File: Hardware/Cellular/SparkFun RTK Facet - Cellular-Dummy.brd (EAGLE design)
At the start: 60 x 30.7 mm, 69 parts, among them IC1 SN74AVC4T774PW, J18 SARA_USB, J2 NANO_SIM, J3 U.FL, J6 DIAG, Q2 310mA/60V/1.6Ω, Q3 310mA/60V/1.6Ω, Q4 310mA/60V/1.6Ω, Q5 20V/0.2A/8MHz/1.2Ω/1Vth, Q7 310mA/60V/1.6Ω, U1 SARA-R510M8S, U8 74HC1G04

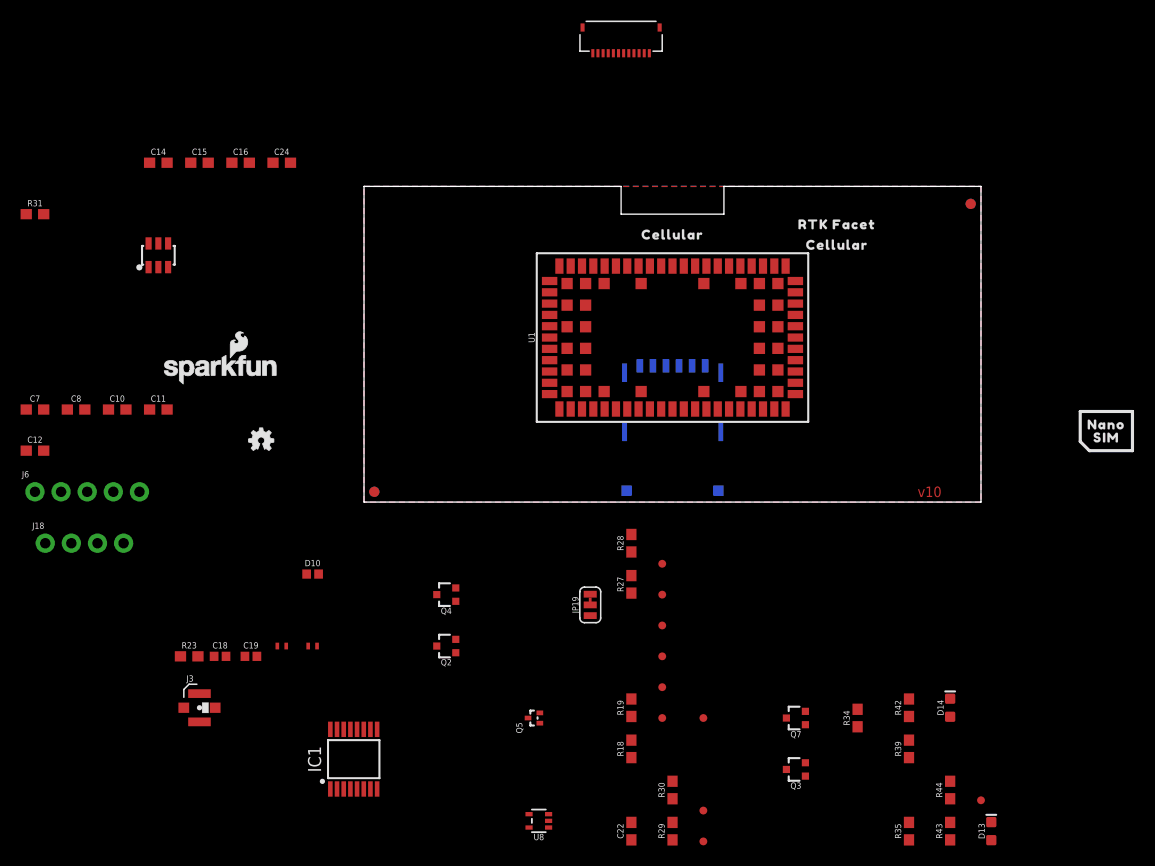
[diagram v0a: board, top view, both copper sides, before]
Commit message: Double up 3.3V on cell connector. Create dummy test board.
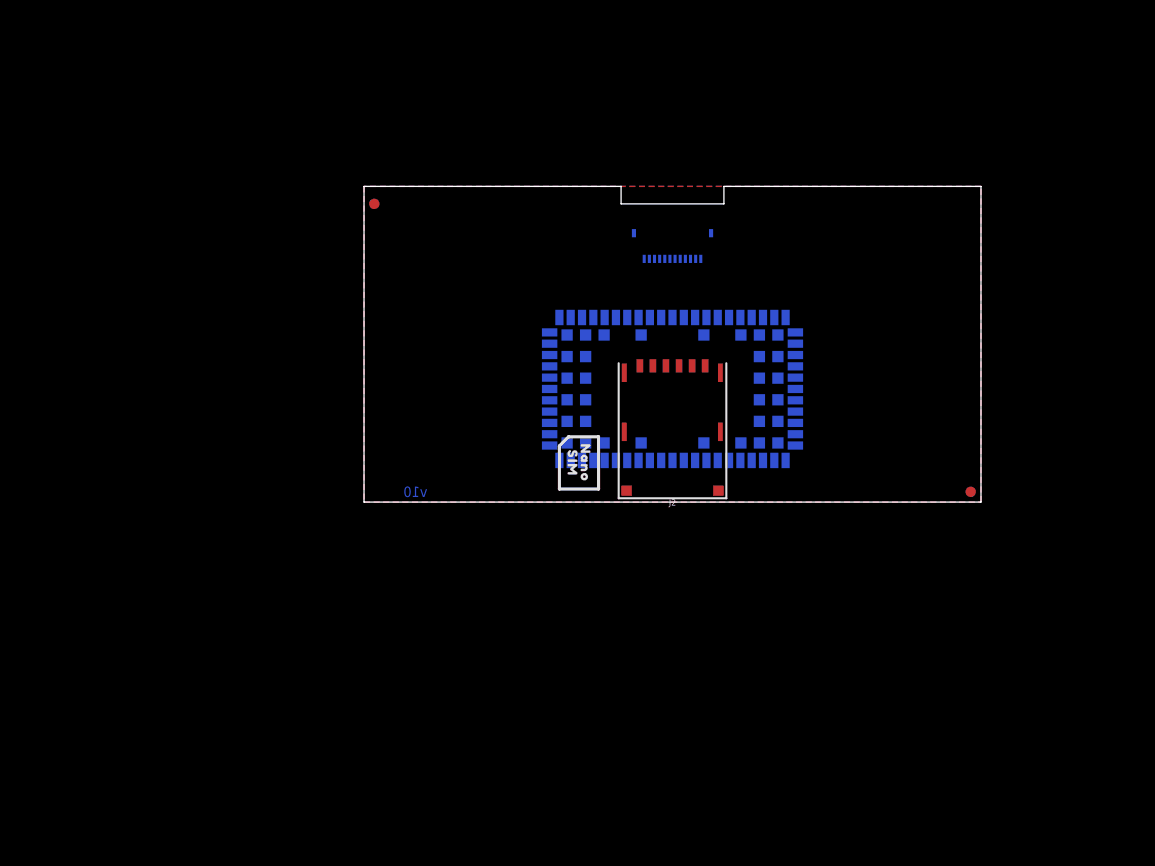
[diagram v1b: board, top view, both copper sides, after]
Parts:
- removed C10, C11, C7, C8: 47pF, SparkFun-Capacitors:0603
- removed C12, C14, C22: 0.1uF, SparkFun-Capacitors:0603
- removed C15: 68pF, SparkFun-Capacitors:0603
- removed C16: 10uF, SparkFun-Capacitors:0603
- removed C18: 33pF, New_Parts:0402
- removed C19: 27pF, New_Parts:0402
- removed C24: 15pF, SparkFun-Capacitors:0603
- removed D10: PESD0402, New_Parts:0402
- removed D13: BLUE, SparkFun-LED:LED-0603
- removed D14: WHITE, SparkFun-LED:LED-0603
- removed D8: DT1042-04SO-7, ublox:SOT23-6L
- removed FRAME2: FRAME-LETTERNO_PACKAGE, SparkFun-Aesthetics:DUMMY
- removed IC1: SN74AVC4T774PW, New_Parts:SOP65P640X120-16N
- removed J18: SARA_USB, SparkFun-Connectors:1X04_NO_SILK
- removed J3: U.FL, SparkFun-Connectors:U.FL
- removed J6: DIAG, SparkFun-Connectors:1X05_NO_SILK
- removed JP19: JUMPER-SMT_3_1-NC_TRACE_SILK, SparkFun-Jumpers:SMT-JUMPER_3_1-NC_TRACE_SILK
- removed L1: DNP, New_Parts:0402_COILCRAFT
- removed L2: 68nH, New_Parts:0402_COILCRAFT
- removed Q2, Q3, Q4, Q7: 310mA/60V/1.6Ω, SparkFun-DiscreteSemi:SOT323
- removed Q5: 20V/0.2A/8MHz/1.2Ω/1Vth, SparkFun-DiscreteSemi:SOT-416FL
- removed R18, R19, R39, R44: 100k, SparkFun-Resistors:0603
- removed R23: 10k, SparkFun-Resistors:0603
- removed R27, R28, R34, R42, R43: 1k, SparkFun-Resistors:0603
- removed R29, R30: 2.2k, SparkFun-Resistors:0603
- removed R31: 0, SparkFun-Resistors:0603
- removed R35: 470, SparkFun-Resistors:0603
- removed TP1, TP12, TP13, TP2, TP3, TP4, TP5, TP6, TP7, TP8: TEST-POINT3, SparkFun-Connectors:PAD.03X.03
- removed U8: 74HC1G04, SparkFun-IC-Logic:SOT353
- J2: value NANO_SIM -> (none); device ublox:NANO_SIM_WURTH_693043020611 -> SparkFun-Connectors:NANO_SIM_WURTH_693043020611
- moved LOGO5 65.9 mm to (50.9, 24.9), flipped to the bottom
- moved LOGO3 64.0 mm to (54.0, 5.00), flipped to the bottom
- moved FID1 58.0 mm to (59.0, 1.00), flipped to the top
- moved FID2 58.0 mm to (1.00, 29.0), flipped to the top
- moved FID3 58.0 mm to (1.00, 29.0), flipped to the bottom
- moved FID4 58.0 mm to (59.0, 1.00), flipped to the bottom
- moved U$131 52.0 mm to (20.3, 3.81), turned to 270 degrees
- moved U$130 50.8 mm to (21.5, 3.81), turned to 270 degrees
- moved FRAME1 45.1 mm to (7.43, -29.5), flipped to the top
- moved U$14 32.0 mm to (14.0, 27.0), flipped to the bottom
- moved U$2 32.0 mm to (14.0, 25.0), flipped to the bottom
- moved J1 20.6 mm to (30.0, 25.0), flipped to the bottom
- moved U1 5.00 mm to (30.0, 11.0), flipped to the bottom
- moved U$13 4.00 mm to (30.0, 22.0), flipped to the bottom
- flipped J2 to the top
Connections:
- removed net 1.8V: J6.4
- removed net LTE_NI: Q3.3, R35.1, R39.1
- removed net N$15: C18.2, J3.FEED, L2.P$2
- removed net N$16: C19.1, D10.1, L2.P$1, R23.2
- removed net N$26: Q2.1, R27.2
- removed net N$27: Q4.1, R28.2
- removed net N$28: R28.1, U8.4
- removed net N$31: R31.2, U1.4
- removed net N$35: Q3.1, R34.2
- removed net N$37: D13.C, R35.2
- removed net N$43: JP19.2, Q5.2, R29.1
- removed net N$47: Q7.1, R42.2
- removed net N$49: D14.C, R43.2
- removed net SARA_!ON!: Q7.3, R43.1, R44.1, TP13.P$1
- removed net SARA_GPIO3: JP19.1
- removed net VCCIO: C22.1, IC1.1, IC1.16, IC1.7, J6.3, Q5.1, R29.2, R31.1, R42.1
- removed net VIN: J6.1
- new net VCC: J2.C1, U1.51, U1.52, U1.53
- net 3.3V: no longer C14.1, C15.1, C16.1, C24.1, D13.A, D14.A, IC1.15, J6.2, R30.2, R39.2, R44.2, U1.51, U1.52, U1.53, U8.5
- net GND: no longer C10.1, C11.1, C12.1, C14.2, C15.2, C16.2, C19.2, C22.2, C24.2, C7.2, C8.2, D10.2, D8.2, D8.5, IC1.10, IC1.2, IC1.8, IC1.9, J18.4, J3.1, J3.2, J6.5, L1.P$2, Q2.2, Q3.2, Q4.2, Q7.2, R18.2, R19.1, U8.3
- net LTE_!RESET!: no longer U8.2
- net LTE_CTSI: no longer IC1.11, R19.2, TP8.P$1
- net LTE_INT: no longer Q5.3, R30.1, TP12.P$1
- net LTE_PWR_ON: no longer R18.1, R27.1
- net LTE_RTSO: no longer IC1.12, TP7.P$1
- net LTE_RXI: no longer IC1.13, TP6.P$1
- net LTE_TXO: no longer IC1.14, TP5.P$1
- net SARA_!RESET!: no longer Q4.3
- net SARA_ANT: no longer C18.1, L1.P$1
- net SARA_ANT_DET: no longer R23.1
- net SARA_CTSO: no longer IC1.5, TP3.P$1
- net SARA_EXT_INT: no longer JP19.3
- net SARA_NI: no longer R34.1
- net SARA_PWR_ON: no longer Q2.3
- net SARA_RTSI: no longer IC1.6, TP4.P$1
- net SARA_RXO: no longer IC1.3, TP1.P$1
- net SARA_TXI: no longer IC1.4, TP2.P$1
- net SARA_USB_D+: no longer J18.2
- net SARA_USB_D-: no longer J18.1
- net SARA_VUSB_DET: no longer J18.3
- net SIM_CLK: no longer C8.1, D8.1, J2.C3
- net SIM_IO: no longer C10.2, D8.6, J2.C7
- net SIM_RST: no longer C7.1, D8.4, J2.C2
- net VSIM: no longer C11.2, C12.2, D8.3, J2.C1
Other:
- outline, holes or cut-outs redrawn

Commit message: Change to push push socket on cellular board.
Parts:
- J2: value (none) -> NANO; device SparkFun-Connectors:NANO_SIM_WURTH_693043020611 -> SparkFun-Connectors:NANO_SIM_PP
- moved J2 1.10 mm to (31.1, 6.90)
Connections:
- new net N$1: J2.C1
- net VCC: no longer J2.C1
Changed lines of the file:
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@@
 <layer number="23" name="tOrigins" color="15" fill="1" visible="yes" active="yes"/>
 <layer number="24" name="bOrigins" color="15" fill="1" visible="yes" active="yes"/>
-<layer number="25" name="tNames" color="7" fill="1" visible="no" active="yes"/>
-<layer number="26" name="bNames" color="7" fill="1" visible="no" active="yes"/>
-<layer number="27" name="tValues" color="7" fill="1" visible="no" active="yes"/>
-<layer number="28" name="bValues" color="7" fill="1" visible="no" active="yes"/>
-<layer number="29" name="tStop" color="7" fill="3" visible="no" active="yes"/>
-<layer number="30" name="bStop" color="7" fill="6" visible="no" active="yes"/>
-<layer number="31" name="tCream" color="7" fill="4" visible="no" active="yes"/>
-<layer number="32" name="bCream" color="7" fill="5" visible="no" active="yes"/>
-<layer number="33" name="tFinish" color="6" fill="3" visible="no" active="yes"/>
-<layer number="34" name="bFinish" color="6" fill="6" visible="no" active="yes"/>
-<layer number="35" name="tGlue" color="7" fill="4" visible="no" active="yes"/>
-<layer number="36" name="bGlue" color="7" fill="5" visible="no" active="yes"/>
-<layer number="37" name="tTest" color="7" fill="1" visible="no" active="yes"/>
-<layer number="38" name="bTest" color="7" fill="1" visible="no" active="yes"/>
-<layer number="39" name="tKeepout" color="4" fill="11" visible="no" active="yes"/>
-<layer number="40" name="bKeepout" color="1" fill="11" visible="no" active="yes"/>
-<layer number="41" name="tRestrict" color="4" fill="10" visible="no" active="yes"/>
-<layer number="42" name="bRestrict" color="1" fill="10" visible="no" active="yes"/>
-<layer number="43" name="vRestrict" color="2" fill="10" visible="no" active="yes"/>
-<layer number="44" name="Drills" color="7" fill="1" visible="no" active="yes"/>
+<layer number="25" name="tNames" color="7" fill="1" visible="yes" active="yes"/>
+<layer number="26" name="bNames" color="7" fill="1" visible="yes" active="yes"/>
+<layer number="27" name="tValues" color="7" fill="1" visible="yes" active="yes"/>
+<layer number="28" name="bValues" color="7" fill="1" visible="yes" active="yes"/>
+<layer number="29" name="tStop" color="7" fill="3" visible="yes" active="yes"/>
+<layer number="30" name="bStop" color="7" fill="6" visible="yes" active="yes"/>
+<layer number="31" name="tCream" color="7" fill="4" visible="yes" active="yes"/>
+<layer number="32" name="bCream" color="7" fill="5" visible="yes" active="yes"/>
+<layer number="33" name="tFinish" color="6" fill="3" visible="yes" active="yes"/>
+<layer number="34" name="bFinish" color="6" fill="6" visible="yes" active="yes"/>
+<layer number="35" name="tGlue" color="7" fill="4" visible="yes" active="yes"/>
+<layer number="36" name="bGlue" color="7" fill="5" visible="yes" active="yes"/>
+<layer number="37" name="tTest" color="7" fill="1" visible="yes" active="yes"/>
+<layer number="38" name="bTest" color="7" fill="1" visible="yes" active="yes"/>
+<layer number="39" name="tKeepout" color="4" fill="11" visible="yes" active="yes"/>
+<layer number="40" name="bKeepout" color="1" fill="11" visible="yes" active="yes"/>
+<layer number="41" name="tRestrict" color="4" fill="10" visible="yes" active="yes"/>
+<layer number="42" name="bRestrict" color="1" fill="10" visible="yes" active="yes"/>
+<layer number="43" name="vRestrict" color="2" fill="10" visible="yes" active="yes"/>
+<layer number="44" name="Drills" color="7" fill="1" visible="yes" active="yes"/>
 <layer number="45" name="Holes" color="7" fill="1" visible="yes" active="yes"/>
 <layer number="46" name="Milling" color="3" fill="1" visible="yes" active="yes"/>
-<layer number="47" name="Measures" color="7" fill="1" visible="no" active="yes"/>
-<layer number="48" name="Document" color="7" fill="1" visible="no" active="yes"/>
-<layer number="49" name="Reference" color="7" fill="1" visible="no" active="yes"/>
-<layer number="50" name="dxf" color="7" fill="1" visible="no" active="yes"/>
+<layer number="47" name="Measures" color="7" fill="1" visible="yes" active="yes"/>
+<layer number="48" name="Document" color="7" fill="1" visible="yes" active="yes"/>
+<layer number="49" name="Reference" color="7" fill="1" visible="yes" active="yes"/>
+<layer number="50" name="dxf" color="7" fill="1" visible="yes" active="yes"/>
 <layer number="51" name="tDocu" color="6" fill="1" visible="yes" active="yes"/>
-<layer number="52" name="bDocu" color="7" fill="1" visible="no" active="yes"/>
+<layer number="52" name="bDocu" color="7" fill="1" visible="yes" active="yes"/>
 <layer number="91" name="Nets" color="2" fill="1" visible="no" active="no"/>
 <layer number="92" name="Busses" color="1" fill="1" visible="no" active="no"/>
@@
 <layer number="56" name="wert" color="7" fill="1" visible="no" active="no"/>
 <layer number="57" name="tCAD" color="7" fill="1" visible="no" active="no"/>
+<layer number="58" name="bCAD" color="7" fill="1" visible="no" active="no"/>
 <layer number="59" name="tCarbon" color="7" fill="1" visible="no" active="no"/>
 <layer number="60" name="bCarbon" color="7" fill="1" visible="no" active="no"/>
@@
 <layer number="250" name="Descript" color="7" fill="1" visible="no" active="no"/>
 <layer number="251" name="SMDround" color="7" fill="1" visible="no" active="no"/>
+<layer number="253" name="Extra" color="7" fill="1" visible="no" active="no"/>
 <layer number="254" name="cooling" color="7" fill="1" visible="no" active="no"/>
 <layer number="255" name="routoute" color="7" fill="1" visible="no" active="no"/>
@@
 <element name="U$130" library="output" package="NANO0" value="" x="21.54" y="3.81" smashed="yes" rot="R270"/>
 <element name="U$131" library="output" package="SIM0" value="" x="20.27" y="3.81" smashed="yes" rot="R270"/>
-<element name="J2" library="SparkFun-Connectors" package="NANO_SIM_WURTH_693043020611" value="" x="30" y="7" smashed="yes">
-<attribute name="NAME" x="30" y="0.269" size="0.6096" layer="25" font="vector" ratio="20" align="top-center"/>
-<attribute name="PROD_ID" value="CONN-14097" x="30" y="7" size="1.778" layer="27" font="vector" display="off"/>
-<attribute name="VALUE" x="30" y="7" size="0.6096" layer="27" font="vector" ratio="20" align="top-center"/>
+<element name="J2" library="SparkFun-Connectors" package="NANO_SIM_PP" value="NANO" x="31.1" y="6.9" smashed="yes">
+<attribute name="NAME" x="31.1" y="7.9" size="0.5" layer="25" align="center"/>
+<attribute name="VALUE" x="31.1" y="6.9" size="0.5" layer="27" align="center"/>
 </element>
 </elements>
@@
 <wire x1="27.75" y1="23.65" x2="27.25" y2="23.65" width="0" layer="19" extent="16-16"/>
 <wire x1="30" y1="17.95" x2="27.75" y2="23.65" width="0" layer="19" extent="16-16"/>
-<wire x1="33.175" y1="13.25" x2="33.05" y2="16.25" width="0" layer="19" extent="1-16"/>
+<wire x1="32.625" y1="14.435" x2="33.05" y2="16.25" width="0" layer="19" extent="1-16"/>
 </signal>
 <signal name="3.3V" class="1">
@@
 <contactref element="U1" pad="52"/>
 <contactref element="U1" pad="53"/>
-<contactref element="J2" pad="C1"/>
 <wire x1="39.9" y1="17.95" x2="41" y2="17.95" width="0" layer="19" extent="16-16"/>
 <wire x1="38.8" y1="17.95" x2="39.9" y2="17.95" width="0" layer="19" extent="16-16"/>
-<wire x1="31.905" y1="13.25" x2="38.8" y2="17.95" width="0" layer="19" extent="1-16"/>
+</signal>
+<signal name="N$1">
+<contactref element="J2" pad="C1"/>
 </signal>
 </signals>
@@
 </board>
 </drawing>
-<compatibility>
-<note version="6.3" minversion="6.2.2" severity="warning">
-Since Version 6.2.2 text objects can contain more than one line,
-which will not be processed correctly with this version.
-</note>
-</compatibility>
 </eagle>
